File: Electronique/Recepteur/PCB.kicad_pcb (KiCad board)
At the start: 2 copper layers, 17.5 x 24.8 mm, 13 parts, among them J1 USB_A, SW3 SW_Push, SW4 SW_Push, U3 ESP32-S3-MINI-1, U4 TLV75533PDBV

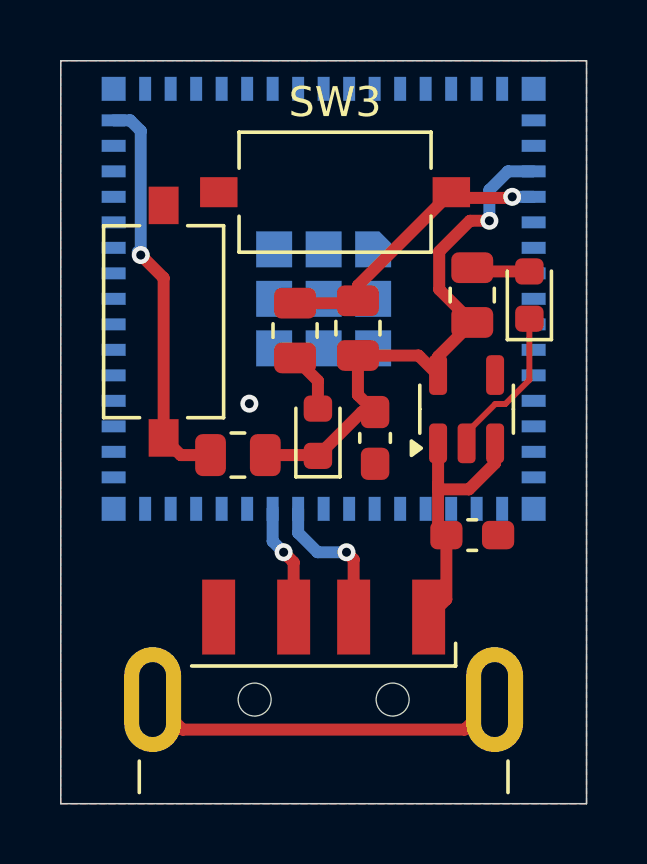
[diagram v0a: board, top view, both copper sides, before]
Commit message: update keyboard schematic
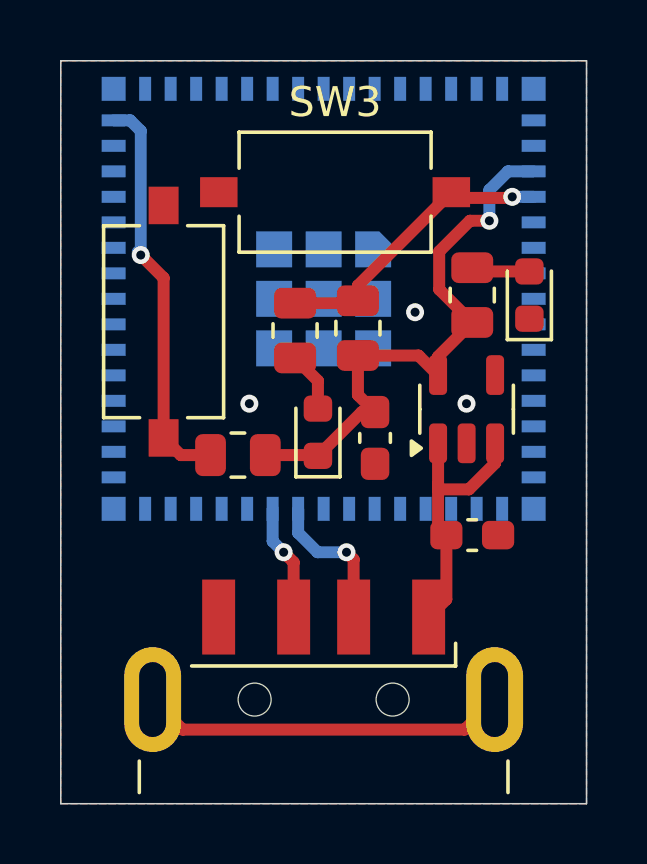
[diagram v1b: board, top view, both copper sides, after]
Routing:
- net GND: track 5.22 -> 0.35 mm, vias 1 -> 3
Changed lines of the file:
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@@
 	)
 	(setup
+		(stackup
+			(layer "F.SilkS"
+				(type "Top Silk Screen")
+			)
+			(layer "F.Paste"
+				(type "Top Solder Paste")
+			)
+			(layer "F.Mask"
+				(type "Top Solder Mask")
+				(thickness 0.01)
+			)
+			(layer "F.Cu"
+				(type "copper")
+				(thickness 0.035)
+			)
+			(layer "dielectric 1"
+				(type "core")
+				(thickness 1.51)
+				(material "FR4")
+				(epsilon_r 4.5)
+				(loss_tangent 0.02)
+			)
+			(layer "B.Cu"
+				(type "copper")
+				(thickness 0.035)
+			)
+			(layer "B.Mask"
+				(type "Bottom Solder Mask")
+				(thickness 0.01)
+			)
+			(layer "B.Paste"
+				(type "Bottom Solder Paste")
+			)
+			(layer "B.SilkS"
+				(type "Bottom Silk Screen")
+			)
+			(copper_finish "None")
+			(dielectric_constraints no)
+		)
 		(pad_to_mask_clearance 0)
 		(allow_soldermask_bridges_in_footprints no)
@@
 	)
 	(segment
-		(start 183.077532 100.7855)
-		(end 183.411468 100.7855)
-		(width 0.2)
-		(layer "F.Cu")
-		(net 1)
-	)
-	(segment
-		(start 182.1205 101.742532)
-		(end 183.077532 100.7855)
-		(width 0.2)
-		(layer "F.Cu")
-		(net 1)
-	)
-	(segment
-		(start 183.411468 100.7855)
-		(end 184.2135 99.983468)
+		(start 182.1205 102.097)
+		(end 182.1205 101.742532)
 		(width 0.2)
 		(layer "F.Cu")
 		(net 1)
 	)
-	(segment
-		(start 184.2135 99.983468)
-		(end 184.2135 97.9425)
-		(width 0.2)
-		(layer "F.Cu")
+	(via
+		(at 182.118 100.7745)
+		(size 0.6)
+		(drill 0.3)
+		(layers "F.Cu" "B.Cu")
+		(free yes)
 		(net 1)
 	)
-	(segment
-		(start 182.1205 102.097)
-		(end 182.1205 101.742532)
-		(width 0.2)
-		(layer "F.Cu")
+	(via
+		(at 174.879 100.7745)
+		(size 0.6)
+		(drill 0.3)
+		(layers "F.Cu" "B.Cu")
+		(free yes)
 		(net 1)
 	)
 	(via
-		(at 174.879 100.7745)
+		(at 180.4035 97.7265)
 		(size 0.6)
 		(drill 0.3)
